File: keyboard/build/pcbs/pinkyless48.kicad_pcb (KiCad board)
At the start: 2 copper layers, 137.9 x 133.1 mm, 51 parts

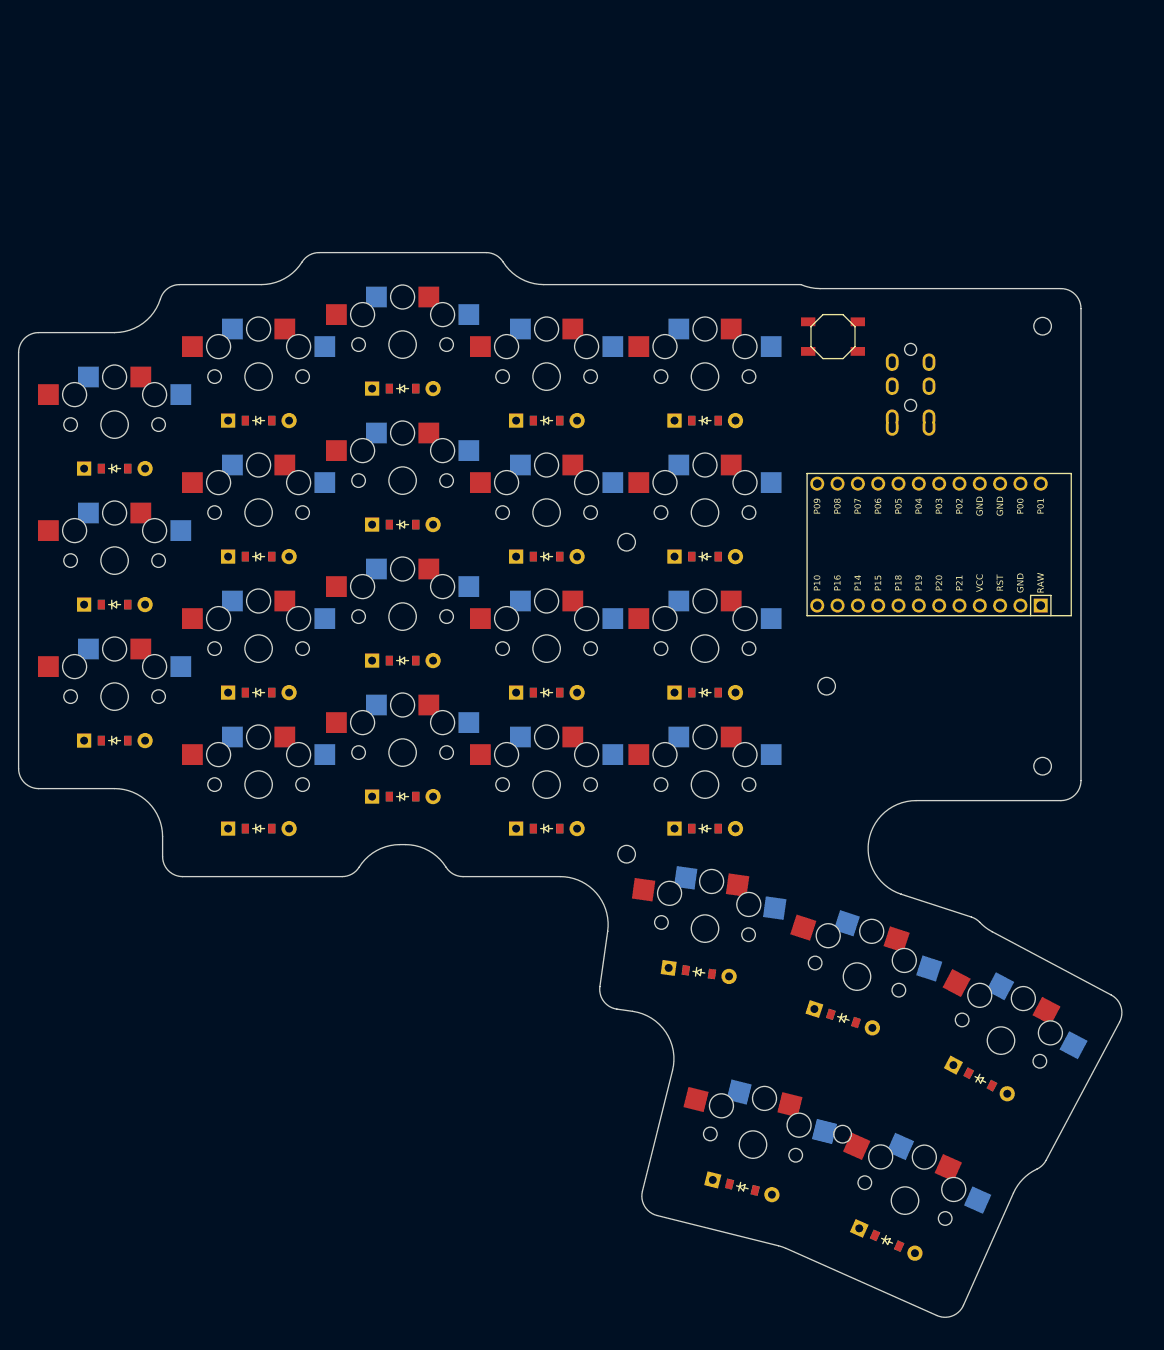
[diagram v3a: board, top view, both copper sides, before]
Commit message: Open up key spacing, fill the inboard bay, enforce clearances
Three related changes, all driven by measurement rather than eyeballing.

Key pitch 18 x 17 -> 18.5 x 18. The Choc standard leaves 0.5 mm between MBK
keycaps in both directions and 2.0 mm between switch base flanges down a
column. That is what stock Choc boards use and it does work, but it is tight
for getting a puller under a cap and leaves nothing for caps larger than MBK.
Now 1.0 mm between caps across columns, 1.5 mm down rows, 3.0 mm between
flanges - for about 2 mm of width and 3 mm of height.

Fixed a real defect this exposed: thumb t1 sat 0.36 mm from the inner
column's bottom keycap and touched outright with 18 x 17 caps, and t2/t3 were
0.85 mm apart - both far tighter than the grid beside them, because rotated
keys lose clearance at their corners. The thumb chains now step a uniform
20.0 mm, which puts every thumb pair exactly level with the grid's own
clearance instead of below it.

Closing radius 6 -> 18, filling the wide concave bay between the controller
area and the thumb cluster so the inboard edge runs straight. Costs ~6 cm2 of
otherwise dead board and nothing in bounding box; narrowest neck goes from
33.0 mm to 55.4 mm.

Two bugs fixed along the way, both mine:

  - The preview outline closed both halves TOGETHER, and at radius 18 that
    bridged the 31 mm gap between them and fused the two halves into one
    shape. The fabricated board was never affected - board_left is the left
    half alone - but the preview picture was wrong. Each half is now closed
    separately before they are unioned.
  - check_outline welded vertices by rounding into fixed buckets, so two
    points a nanometre apart could straddle a bucket boundary and be reported
    as dangling endpoints on a perfectly closed outline. Welding now searches
    neighbouring buckets, and zero-length segments from arc sampling are
    dropped.

check_layout now enforces MINIMUM gaps rather than merely absence of overlap,
for b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
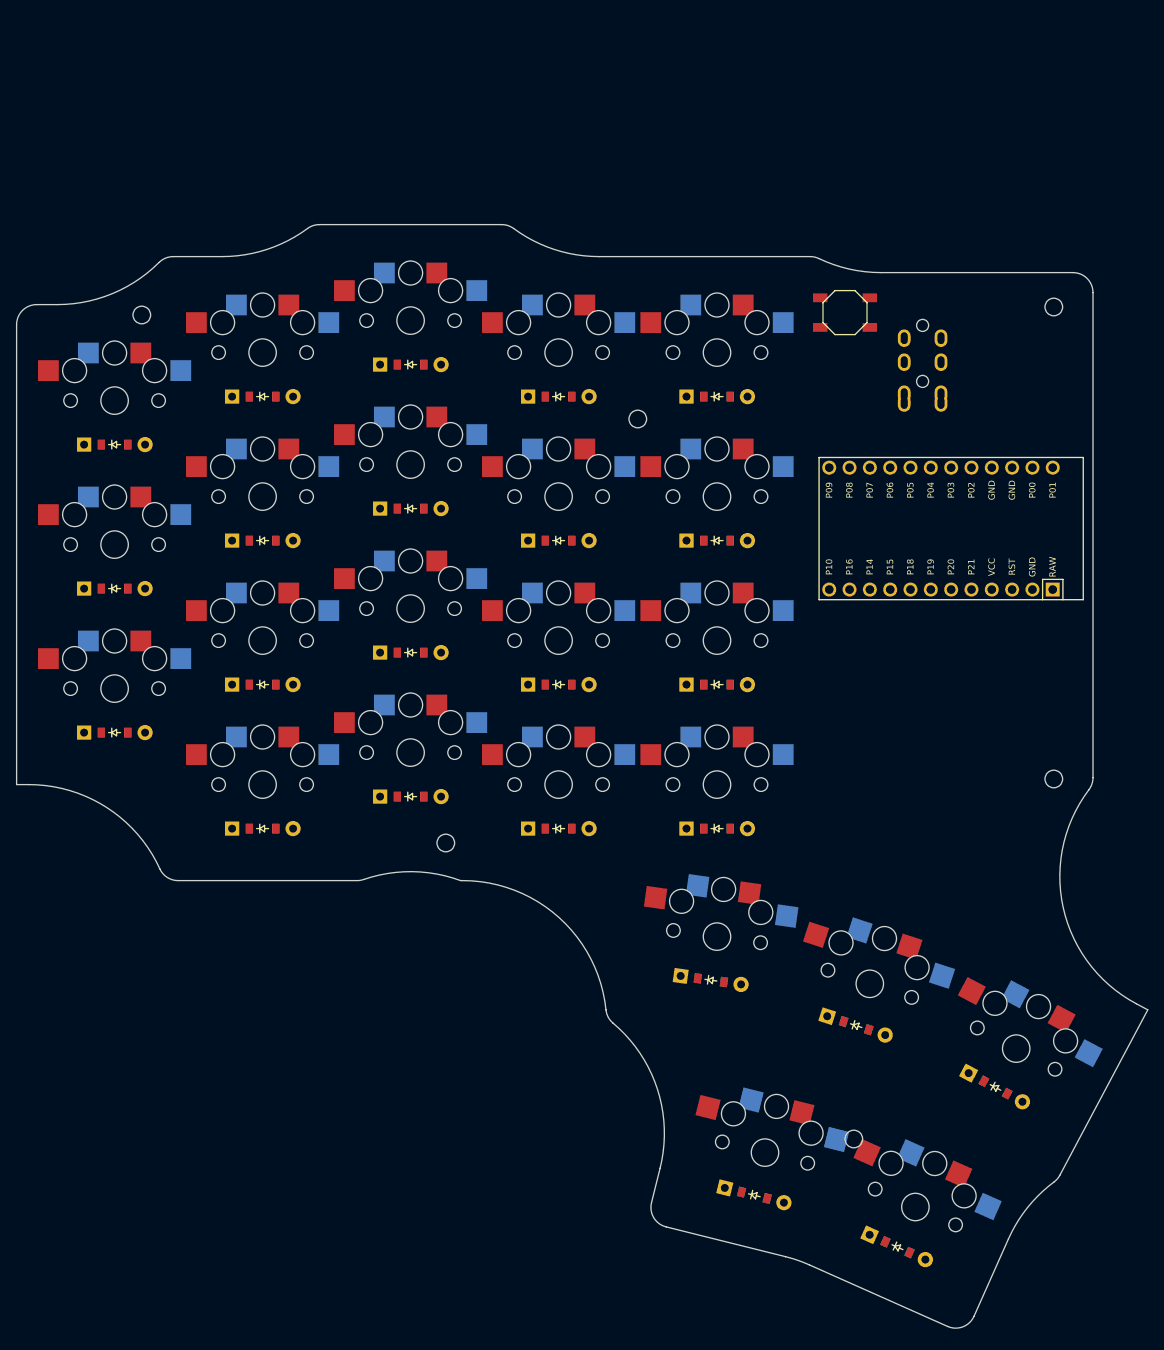
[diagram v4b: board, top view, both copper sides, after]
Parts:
- moved B1 3.35 mm to (151.3, 101.0)
- moved D15 3.35 mm to (115.5, 111.5)
- moved D19 3.35 mm to (135.3, 111.5)
- moved S15 3.35 mm to (115.5, 106.0)
- moved S19 3.35 mm to (135.3, 106.0)
- moved TRRS1 3.35 mm to (163.3, 101.0)
- moved D11 3.16 mm to (97.0, 107.5)
- moved S11 3.16 mm to (97.0, 102.0)
- moved D7 3.04 mm to (78.5, 111.5)
- moved S7 3.04 mm to (78.5, 106.0)
- moved D3 3.00 mm to (60.0, 117.5)
- moved S3 3.00 mm to (60.0, 112.0)
- moved D14 2.50 mm to (115.5, 129.5)
- moved D18 2.50 mm to (135.3, 129.5)
- moved MCU1 2.50 mm to (163.3, 128.0)
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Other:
- board size 137.9 x 133.1 mm -> 141.4 x 137.9 mm

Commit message: Drop the pinky column further, to 12 mm below the baseline
The stagger was being applied correctly - every pinky key sat 6 mm lower than
its neighbours - but the column still read as sitting HIGHER than the rest.
The cause is not the stagger: the pinky carries three keys and skips the
BOTTOM row, so its block occupies the upper three row positions and its
lowest key ended 12 mm above every other column's lowest key.

Doubling the stagger to 12 mm below the baseline (16 mm below middle) brings
the whole block down: the pinky's lowest key is now 6 mm above the others
rather than 12, and its top key sits 12 mm below theirs. The column now reads
as the lowest one, which is what a short finger wants.

Screw positions re-derived. Case STLs and previews regenerated. All five
checks pass.

Co-Authored-By: Claude Opus 5 <noreply@anthropic.com>
Claude-Session: https://claude.ai/code/session_01TKXtddA7pBLooPYbDwxvxo
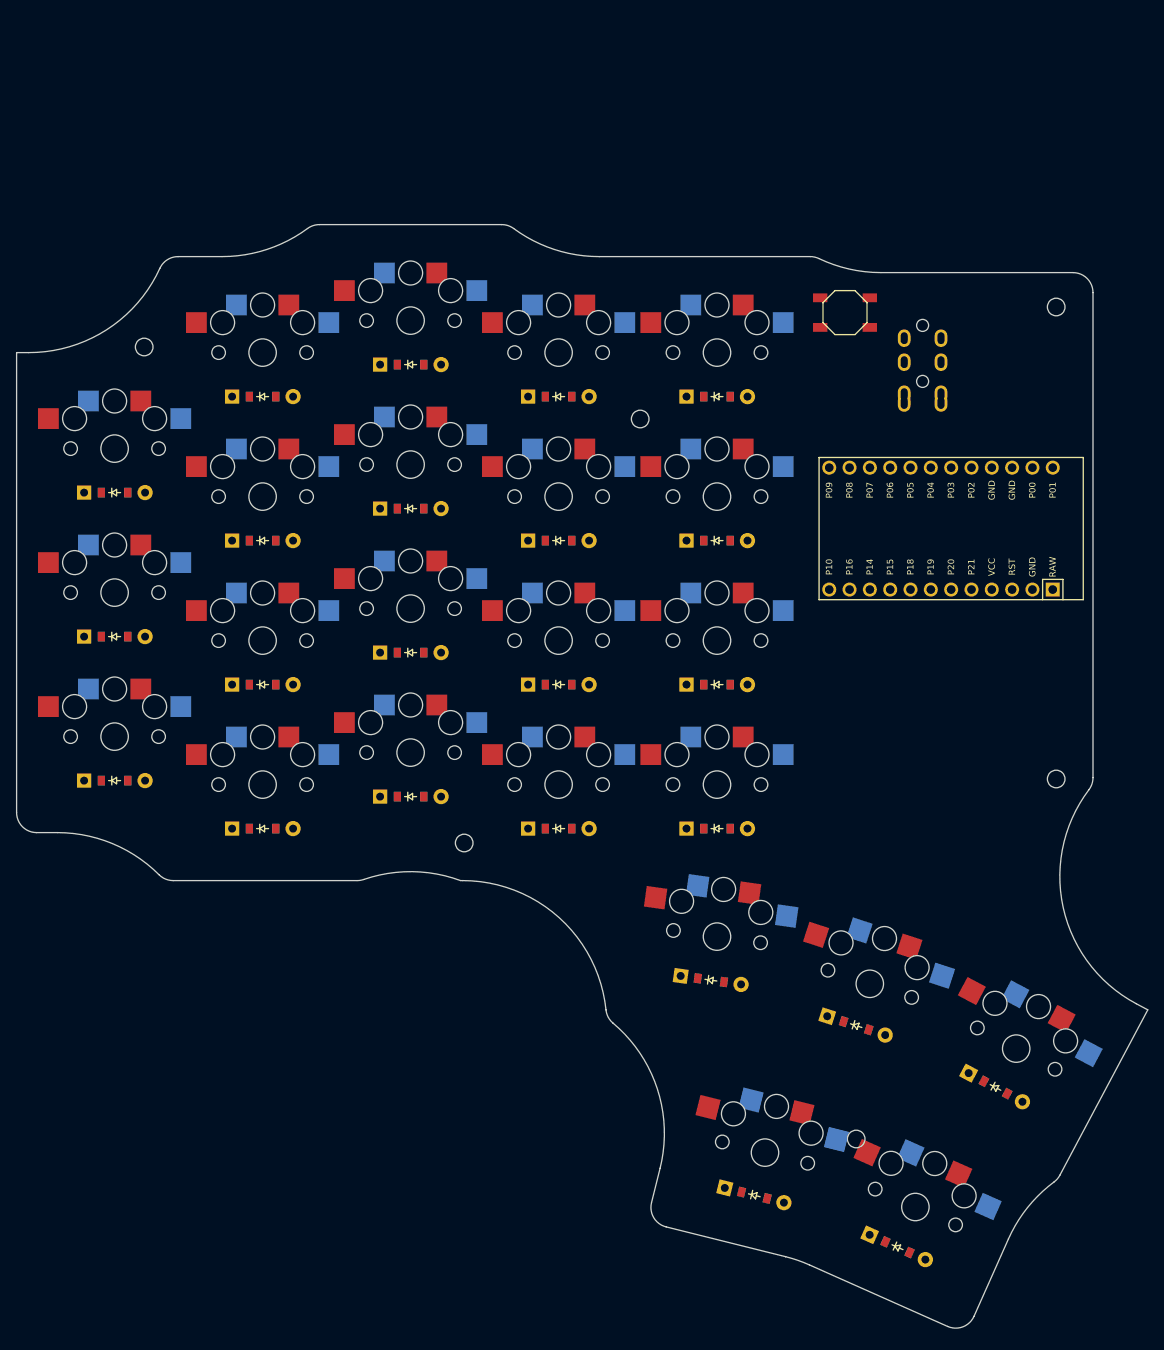
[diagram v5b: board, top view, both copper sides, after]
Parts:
- moved D1 6.00 mm to (60.0, 159.5)
- moved D2 6.00 mm to (60.0, 141.5)
- moved D3 6.00 mm to (60.0, 123.5)
- moved S1 6.00 mm to (60.0, 154.0)
- moved S2 6.00 mm to (60.0, 136.0)
- moved S3 6.00 mm to (60.0, 118.0)
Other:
- outline, holes or cut-outs redrawn
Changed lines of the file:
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@@
   )
       (module PG1350 (layer F.Cu)
-      (at 60 148 0)
+      (at 60 154 0)
       (fp_text reference "S1" (at 0 0) (layer F.SilkS) hide (effects (font (size 1.27 1.27) (thickness 0.15))))
       (fp_text value "" (at 0 0) (layer F.SilkS) hide (effects (font (size 1.27 1.27) (thickness 0.15))))
@@
         )
       (module PG1350 (layer F.Cu)
-      (at 60 130 0)
+      (at 60 136 0)
       (fp_text reference "S2" (at 0 0) (layer F.SilkS) hide (effects (font (size 1.27 1.27) (thickness 0.15))))
       (fp_text value "" (at 0 0) (layer F.SilkS) hide (effects (font (size 1.27 1.27) (thickness 0.15))))
@@
         )
       (module PG1350 (layer F.Cu)
-      (at 60 112 0)
+      (at 60 118 0)
       (fp_text reference "S3" (at 0 0) (layer F.SilkS) hide (effects (font (size 1.27 1.27) (thickness 0.15))))
       (fp_text value "" (at 0 0) (layer F.SilkS) hide (effects (font (size 1.27 1.27) (thickness 0.15))))
@@
         )
     (module ComboDiode (layer F.Cu)
-        (at 60 153.5 0)
+        (at 60 159.5 0)
         (fp_text reference "D1" (at 0 0) (layer F.SilkS) hide (effects (font (size 1.27 1.27) (thickness 0.15))))
         (fp_text value "" (at 0 0) (layer F.SilkS) hide (effects (font (size 1.27 1.27) (thickness 0.15))))
@@
     )
     (module ComboDiode (layer F.Cu)
-        (at 60 135.5 0)
+        (at 60 141.5 0)
         (fp_text reference "D2" (at 0 0) (layer F.SilkS) hide (effects (font (size 1.27 1.27) (thickness 0.15))))
         (fp_text value "" (at 0 0) (layer F.SilkS) hide (effects (font (size 1.27 1.27) (thickness 0.15))))
@@
     )
     (module ComboDiode (layer F.Cu)
-        (at 60 117.5 0)
+        (at 60 123.5 0)
         (fp_text reference "D3" (at 0 0) (layer F.SilkS) hide (effects (font (size 1.27 1.27) (thickness 0.15))))
         (fp_text value "" (at 0 0) (layer F.SilkS) hide (effects (font (size 1.27 1.27) (thickness 0.15))))
@@
         (pad 2 smd rect (at 3.1 1.85 0) (size 1.8 1.1) (layers F.Cu F.Paste F.Mask) (net 36 "GND"))
     )
-  (gr_line (start 47.75 160) (end 49.279437200000004 160) (angle 90) (layer Edge.Cuts) (width 0.15))
-(gr_arc (start 49.279437200000004 178) (end 65.6592248 170.5365854) (angle -65.50372094166269) (layer Edge.Cuts) (width 0.15))
-(gr_line (start 67.9341953 172) (end 90.3170334 172) (angle 90) (layer Edge.Cuts) (width 0.15))
+  (gr_line (start 50.25 166) (end 52.833592100000004 166) (angle 90) (layer Edge.Cuts) (width 0.15))
+(gr_arc (start 52.833592100000004 184) (end 65.55772780000001 171.2682927) (angle -44.98295773650154) (layer Edge.Cuts) (width 0.15))
+(gr_line (start 67.32496880000001 172) (end 90.3170334 172) (angle 90) (layer Edge.Cuts) (width 0.15))
 (gr_arc (start 97 188.8800918) (end 103.25 172) (angle -39.343579589725564) (layer Edge.Cuts) (width 0.15))
 (gr_line (start 103.25 172) (end 103.5179019 172) (angle 90) (layer Edge.Cuts) (width 0.15))
@@
 (gr_line (start 108.39818340000001 90) (end 85.60181659999999 90) (angle 90) (layer Edge.Cuts) (width 0.15))
 (gr_arc (start 73.4362915 76) (end 73.4362915 94) (angle -36.40152061770755) (layer Edge.Cuts) (width 0.15))
-(gr_line (start 73.4362915 94) (end 67.32496880000001 94) (angle 90) (layer Edge.Cuts) (width 0.15))
-(gr_arc (start 52.833592100000004 82) (end 52.833592100000004 100) (angle -44.98295773650153) (layer Edge.Cuts) (width 0.15))
-(gr_line (start 52.833592100000004 100) (end 50.25 100) (angle 90) (layer Edge.Cuts) (width 0.15))
-(gr_line (start 47.75 160) (end 47.75 102.5) (angle 90) (layer Edge.Cuts) (width 0.15))
-(gr_arc (start 67.9341953 169.5) (end 65.6592248 170.5365854) (angle -65.50372094166269) (layer Edge.Cuts) (width 0.15))
+(gr_line (start 73.4362915 94) (end 67.9341953 94) (angle 90) (layer Edge.Cuts) (width 0.15))
+(gr_arc (start 49.279437200000004 88) (end 49.279437200000004 106) (angle -65.50372094166266) (layer Edge.Cuts) (width 0.15))
+(gr_line (start 49.279437200000004 106) (end 47.75000000000001 106) (angle 90) (layer Edge.Cuts) (width 0.15))
+(gr_line (start 47.75 163.5) (end 47.75 106) (angle 90) (layer Edge.Cuts) (width 0.15))
+(gr_arc (start 67.32496880000001 169.5) (end 65.5577277 171.2682927) (angle -44.98295773650153) (layer Edge.Cuts) (width 0.15))
 (gr_arc (start 90.3170334 169.5) (end 90.3170334 172) (angle -19.026071927930843) (layer Edge.Cuts) (width 0.15))
 (gr_arc (start 123.910125 187.9006579) (end 121.42326849999999 188.1566752) (angle -44.086622016723254) (layer Edge.Cuts) (width 0.15))
@@
 (gr_arc (start 108.39818340000001 92.5) (end 109.88178400000001 90.4878049) (angle -36.40152061770755) (layer Edge.Cuts) (width 0.15))
 (gr_arc (start 85.60181659999999 92.5) (end 85.60181659999999 90) (angle -36.40152061770755) (layer Edge.Cuts) (width 0.15))
-(gr_arc (start 67.32496880000001 96.5) (end 67.32496880000001 94) (angle -44.98295773650153) (layer Edge.Cuts) (width 0.15))
-(gr_arc (start 50.25 102.5) (end 50.25 100) (angle -90) (layer Edge.Cuts) (width 0.15))
-(gr_circle (center 177.4 100.3) (end 178.5 100.3) (layer Edge.Cuts) (width 0.15))
-(gr_circle (center 63.4 101.3) (end 64.5 101.3) (layer Edge.Cuts) (width 0.15))
-(gr_circle (center 125.4 114.3) (end 126.5 114.3) (layer Edge.Cuts) (width 0.15))
-(gr_circle (center 177.4 159.3) (end 178.5 159.3) (layer Edge.Cuts) (width 0.15))
-(gr_circle (center 101.4 167.3) (end 102.5 167.3) (layer Edge.Cuts) (width 0.15))
-(gr_circle (center 152.4 204.3) (end 153.5 204.3) (layer Edge.Cuts) (width 0.15))
+(gr_arc (start 67.9341953 96.5) (end 67.9341953 94) (angle -65.50372094166269) (layer Edge.Cuts) (width 0.15))
+(gr_arc (start 50.25 163.5) (end 47.75 163.5) (angle -90) (layer Edge.Cuts) (width 0.15))
+(gr_circle (center 177.7 100.3) (end 178.79999999999998 100.3) (layer Edge.Cuts) (width 0.15))
+(gr_circle (center 63.7 105.3) (end 64.8 105.3) (layer Edge.Cuts) (width 0.15))
+(gr_circle (center 125.7 114.3) (end 126.8 114.3) (layer Edge.Cuts) (width 0.15))
+(gr_circle (center 177.7 159.3) (end 178.79999999999998 159.3) (layer Edge.Cuts) (width 0.15))
+(gr_circle (center 103.7 167.3) (end 104.8 167.3) (layer Edge.Cuts) (width 0.15))
+(gr_circle (center 152.7 204.3) (end 153.79999999999998 204.3) (layer Edge.Cuts) (width 0.15))
 )
